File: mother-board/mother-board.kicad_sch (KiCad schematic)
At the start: 23 parts, among them J1 Screw_Terminal_01x02, J10 Screw_Terminal_01x02, J2 Screw_Terminal_01x02, J3 Screw_Terminal_01x02, J4 Screw_Terminal_01x02, J5 Screw_Terminal_01x02, J6 Screw_Terminal_01x02, J7 Screw_Terminal_01x02, J8 Screw_Terminal_01x02, J9 Conn_02x03_Odd_Even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

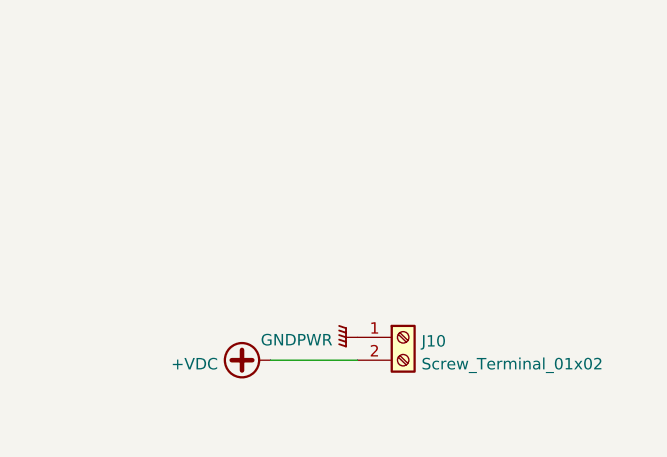
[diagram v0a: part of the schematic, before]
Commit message: add all footprints and netlist
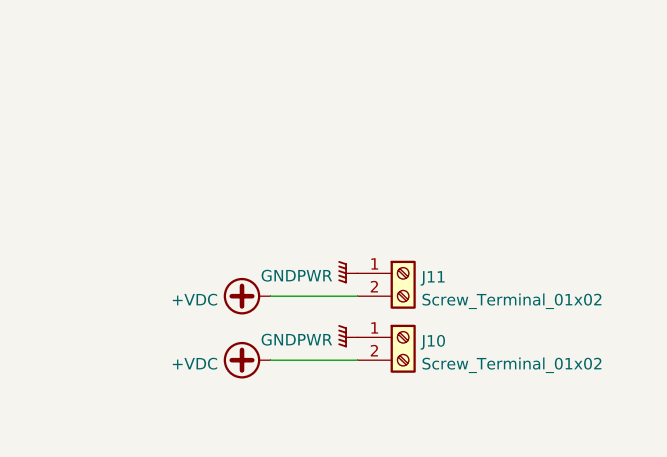
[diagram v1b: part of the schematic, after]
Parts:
- added J11: Screw_Terminal_01x02, TerminalBlock:TerminalBlock_bornier-2_P5.08mm, symbol Connector:Screw_Terminal_01x02
- J9: footprint (none) -> Connector_IDC:IDC-Header_2x03_P2.54mm_Vertical
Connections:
- net +VDC: now also J11.2 (Pin_2)
- net GNDPWR: now also J11.1 (Pin_1)
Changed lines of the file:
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@@
+    (stroke (width 0) (type default) (color 0 0 0 0))
+  )
+  (wire (pts (xy 244.094 133.35) (xy 253.746 133.35))
     (stroke (width 0) (type default) (color 0 0 0 0))
   )
@@
     (property "Reference" "J9" (id 0) (at 218.44 71.9582 0))
     (property "Value" "Conn_02x03_Odd_Even" (id 1) (at 218.44 74.2696 0))
-    (property "Footprint" "" (id 2) (at 217.17 80.01 0)
+    (property "Footprint" "Connector_IDC:IDC-Header_2x03_P2.54mm_Vertical" (id 2) (at 217.17 80.01 0)
       (effects (font (size 1.27 1.27)) hide)
     )
@@
     (pin "3")
   )
+  (symbol (lib_name "GNDPWR_3") (lib_id "power:GNDPWR") (at 253.746 130.81 270) (unit 1)
+    (in_bom yes) (on_board yes) (fields_autoplaced)
+    (property "Reference" "#PWR033" (id 0) (at 248.666 130.81 0)
+      (effects (font (size 1.27 1.27)) hide)
+    )
+    (property "Value" "GNDPWR" (id 1) (at 250.9775 131.1168 90)
+      (effects (font (size 1.27 1.27)) (justify right))
+    )
+    (property "Footprint" "" (id 2) (at 252.476 130.81 0)
+      (effects (font (size 1.27 1.27)) hide)
+    )
+    (property "Datasheet" "" (id 3) (at 252.476 130.81 0)
+      (effects (font (size 1.27 1.27)) hide)
+    )
+    (pin "1")
+  )
+  (symbol (lib_id "Connector:Screw_Terminal_01x02") (at 258.826 130.81 0) (unit 1)
+    (in_bom yes) (on_board yes) (fields_autoplaced)
+    (property "Reference" "J11" (id 0) (at 260.858 131.2453 0)
+      (effects (font (size 1.27 1.27)) (justify left))
+    )
+    (property "Value" "Screw_Terminal_01x02" (id 1) (at 260.858 133.7822 0)
+      (effects (font (size 1.27 1.27)) (justify left))
+    )
+    (property "Footprint" "TerminalBlock:TerminalBlock_bornier-2_P5.08mm" (id 2) (at 258.826 130.81 0)
+      (effects (font (size 1.27 1.27)) hide)
+    )
+    (property "Datasheet" "~" (id 3) (at 258.826 130.81 0)
+      (effects (font (size 1.27 1.27)) hide)
+    )
+    (pin "1")
+    (pin "2")
+  )
   (symbol (lib_name "+5V_1") (lib_id "power:+5V") (at 135.89 38.1 90) (unit 1)
     (in_bom yes) (on_board yes) (fields_autoplaced)
@@
     (pin "2")
   )
+  (symbol (lib_id "power:+VDC") (at 244.094 133.35 90) (unit 1)
+    (in_bom yes) (on_board yes) (fields_autoplaced)
+    (property "Reference" "#PWR032" (id 0) (at 246.634 133.35 0)
+      (effects (font (size 1.27 1.27)) hide)
+    )
+    (property "Value" "+VDC" (id 1) (at 238.252 133.7838 90)
+      (effects (font (size 1.27 1.27)) (justify left))
+    )
+    (property "Footprint" "" (id 2) (at 244.094 133.35 0)
+      (effects (font (size 1.27 1.27)) hide)
+    )
+    (property "Datasheet" "" (id 3) (at 244.094 133.35 0)
+      (effects (font (size 1.27 1.27)) hide)
+    )
+    (pin "1")
+  )
   (symbol (lib_id "Device:LED") (at 72.39 115.57 0) (mirror y) (unit 1)
     (in_bom yes) (on_board yes) (fields_autoplaced)
@@
       (reference "#PWR031") (unit 1) (value "VCC") (footprint "")
     )
+    (path "/a888b96a-e1c5-4002-a181-617c900a21e2"
+      (reference "#PWR032") (unit 1) (value "+VDC") (footprint "")
+    )
+    (path "/64ed324b-a11f-48b8-84cf-73ff8b449458"
+      (reference "#PWR033") (unit 1) (value "GNDPWR") (footprint "")
+    )
     (path "/c34a4246-a310-4cf0-b2fd-6f691dd1754e"
       (reference "#PWR0101") (unit 1) (value "GNDPWR") (footprint "")
@@
     )
     (path "/00000000-0000-0000-0000-0000621d4ee2"
-      (reference "J9") (unit 1) (value "Conn_02x03_Odd_Even") (footprint "")
+      (reference "J9") (unit 1) (value "Conn_02x03_Odd_Even") (footprint "Connector_IDC:IDC-Header_2x03_P2.54mm_Vertical")
     )
     (path "/03631ccf-70f9-40da-a0be-fafec9c829f9"
       (reference "J10") (unit 1) (value "Screw_Terminal_01x02") (footprint "TerminalBlock:TerminalBlock_bornier-2_P5.08mm")
     )
+    (path "/7212aa0a-5a8c-4992-affd-3792f79a39f7"
+      (reference "J11") (unit 1) (value "Screw_Terminal_01x02") (footprint "TerminalBlock:TerminalBlock_bornier-2_P5.08mm")
+    )
     (path "/31a5a69a-f6d6-4422-9e9c-66acea757080"
